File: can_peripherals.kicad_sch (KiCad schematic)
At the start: 14 parts, among them U1 MCP2515, U2 MCP2551, Y1 ABLS7M-16.000MHZ-B-2-T

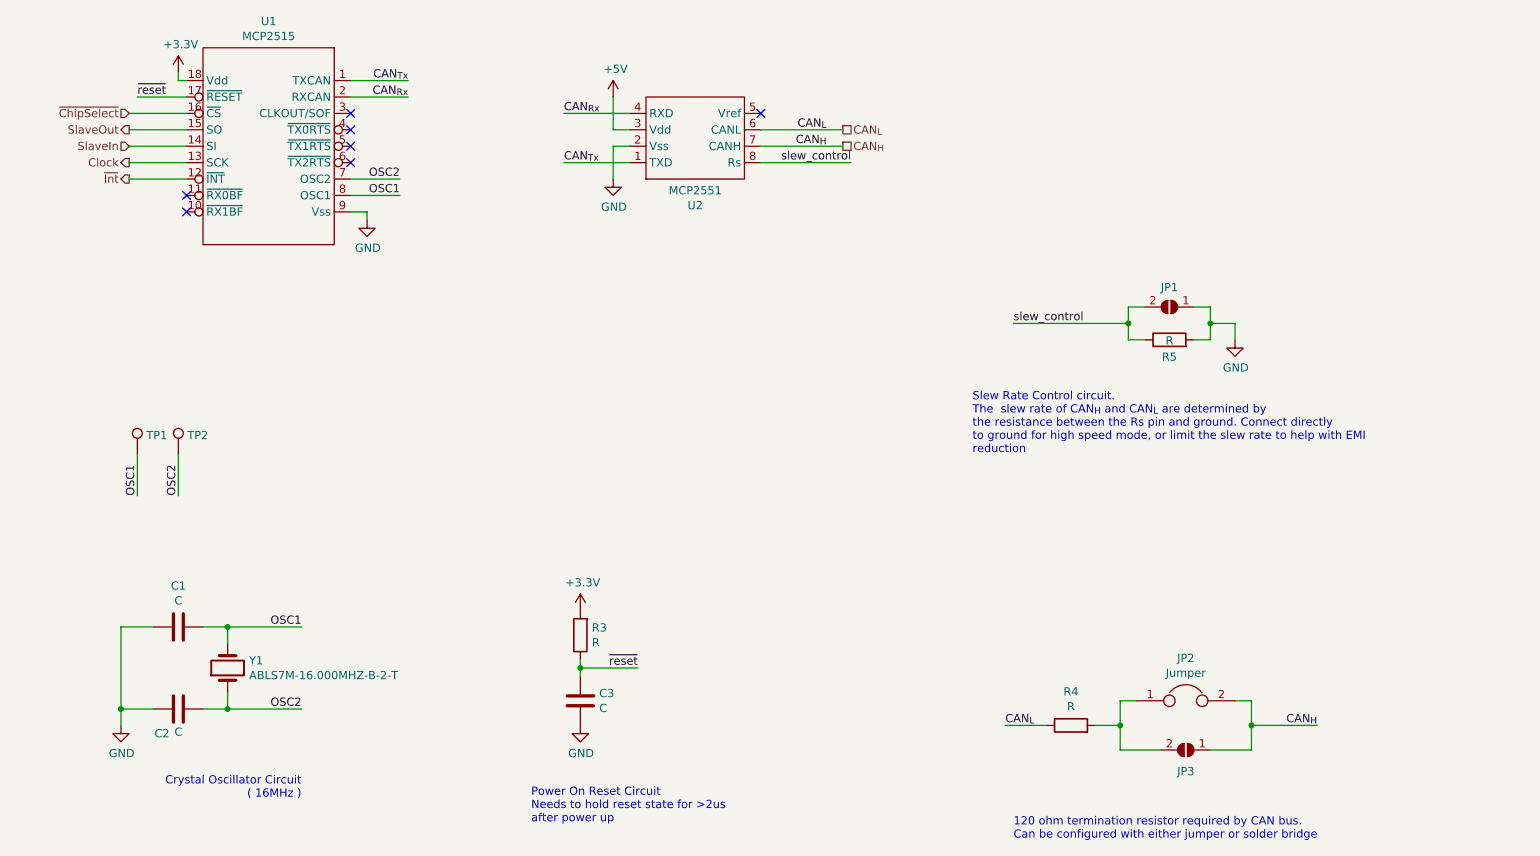
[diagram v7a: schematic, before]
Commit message: more layout: power supply and gpio
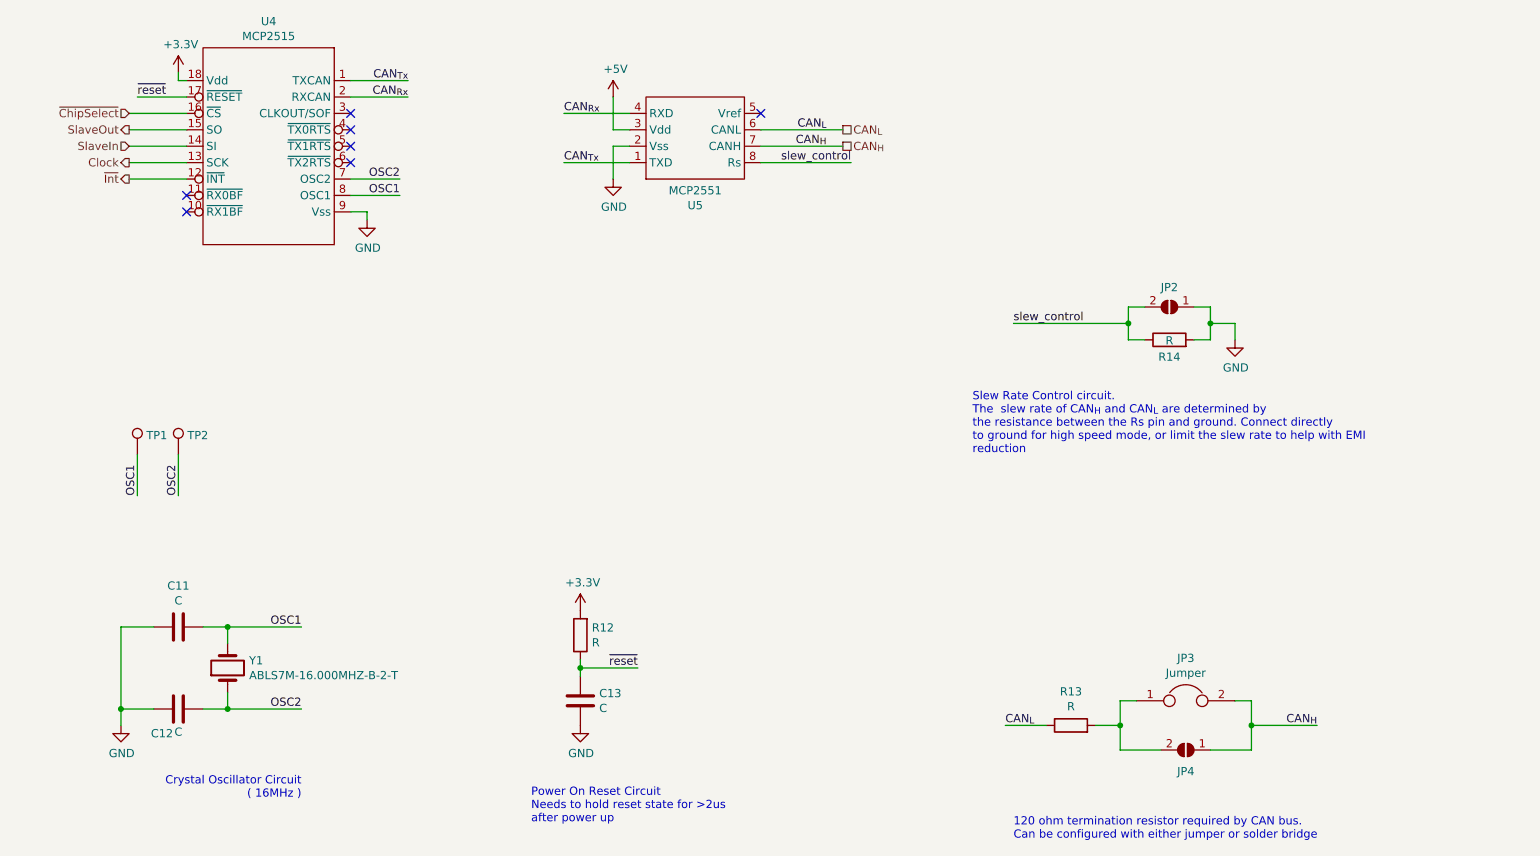
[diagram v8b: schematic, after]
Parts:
- renumbered C1 to C11, C2 to C12, C3 to C13, JP1 to JP2, JP2 to JP3, JP3 to JP4, R3 to R12, R4 to R13, R5 to R14, U1 to U4, U2 to U5
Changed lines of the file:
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@@
   (junction (at 208.026 71.882) (diameter 0.9144) (color 0 0 0 0))
   (junction (at 214.376 134.112) (diameter 0.9144) (color 0 0 0 0))
+  (no_connect (at 49.53 54.61))
+  (no_connect (at 74.93 44.45))
+  (no_connect (at 74.93 41.91))
+  (no_connect (at 74.93 39.37))
+  (no_connect (at 74.93 46.99))
+  (no_connect (at 49.53 52.07))
   (no_connect (at 138.43 39.37))
-  (no_connect (at 74.93 41.91))
-  (no_connect (at 74.93 46.99))
-  (no_connect (at 74.93 39.37))
-  (no_connect (at 49.53 52.07))
-  (no_connect (at 74.93 44.45))
-  (no_connect (at 49.53 54.61))
   (wire (pts (xy 39.37 118.872) (xy 39.37 131.572))
     (stroke (width 0) (type solid) (color 0 0 0 0))
@@
   (symbol (lib_id "power:+3.3V") (at 48.26 33.02 0) (unit 1)
     (in_bom yes) (on_board yes)
-    (property "Reference" "#PWR0113" (id 0) (at 48.26 36.83 0)
+    (property "Reference" "#PWR0148" (id 0) (at 48.26 36.83 0)
       (effects (font (size 1.27 1.27)) hide)
     )
@@
   (symbol (lib_id "power:+3.3V") (at 110.49 116.332 0) (unit 1)
     (in_bom yes) (on_board yes)
-    (property "Reference" "#PWR0118" (id 0) (at 110.49 120.142 0)
+    (property "Reference" "#PWR0144" (id 0) (at 110.49 120.142 0)
       (effects (font (size 1.27 1.27)) hide)
     )
@@
   (symbol (lib_id "power:+5V") (at 115.57 36.83 0) (unit 1)
     (in_bom yes) (on_board yes)
-    (property "Reference" "#PWR0116" (id 0) (at 115.57 40.64 0)
+    (property "Reference" "#PWR0147" (id 0) (at 115.57 40.64 0)
       (effects (font (size 1.27 1.27)) hide)
     )
@@
   (symbol (lib_id "power:GND") (at 39.37 134.112 0) (unit 1)
     (in_bom yes) (on_board yes)
-    (property "Reference" "#PWR0114" (id 0) (at 39.37 140.462 0)
+    (property "Reference" "#PWR0142" (id 0) (at 39.37 140.462 0)
       (effects (font (size 1.27 1.27)) hide)
     )
@@
   (symbol (lib_id "power:GND") (at 77.47 55.88 0) (unit 1)
     (in_bom yes) (on_board yes)
-    (property "Reference" "#PWR0119" (id 0) (at 77.47 62.23 0)
+    (property "Reference" "#PWR0145" (id 0) (at 77.47 62.23 0)
       (effects (font (size 1.27 1.27)) hide)
     )
@@
   (symbol (lib_id "power:GND") (at 110.49 134.112 0) (unit 1)
     (in_bom yes) (on_board yes)
-    (property "Reference" "#PWR0117" (id 0) (at 110.49 140.462 0)
+    (property "Reference" "#PWR0143" (id 0) (at 110.49 140.462 0)
       (effects (font (size 1.27 1.27)) hide)
     )
@@
   (symbol (lib_id "power:GND") (at 115.57 49.53 0) (unit 1)
     (in_bom yes) (on_board yes)
-    (property "Reference" "#PWR0115" (id 0) (at 115.57 55.88 0)
+    (property "Reference" "#PWR0146" (id 0) (at 115.57 55.88 0)
       (effects (font (size 1.27 1.27)) hide)
     )
@@
   (symbol (lib_id "power:GND") (at 211.836 74.422 0) (unit 1)
     (in_bom yes) (on_board yes)
-    (property "Reference" "#PWR0112" (id 0) (at 211.836 80.772 0)
+    (property "Reference" "#PWR0141" (id 0) (at 211.836 80.772 0)
       (effects (font (size 1.27 1.27)) hide)
     )
@@
   (symbol (lib_id "Device:R") (at 110.49 120.142 180) (unit 1)
     (in_bom yes) (on_board yes)
-    (property "Reference" "R3" (id 0) (at 112.2681 118.9926 0)
+    (property "Reference" "R12" (id 0) (at 112.2681 118.9926 0)
       (effects (font (size 1.27 1.27)) (justify right))
     )
@@
   (symbol (lib_id "Device:R") (at 186.436 134.112 90) (unit 1)
     (in_bom yes) (on_board yes)
-    (property "Reference" "R4" (id 0) (at 186.436 128.8858 90))
+    (property "Reference" "R13" (id 0) (at 186.436 128.8858 90))
     (property "Value" "R" (id 1) (at 186.436 131.1845 90))
     (property "Footprint" "Resistor_SMD:R_0805_2012Metric" (id 2) (at 186.436 135.89 90)
@@
   (symbol (lib_id "Device:R") (at 201.676 74.422 90) (unit 1)
     (in_bom yes) (on_board yes)
-    (property "Reference" "R5" (id 0) (at 201.676 77.0698 90))
+    (property "Reference" "R14" (id 0) (at 201.676 77.0698 90))
     (property "Value" "R" (id 1) (at 201.676 74.5425 90))
     (property "Footprint" "Resistor_SMD:R_0805_2012Metric" (id 2) (at 201.676 76.2 90)
@@
   (symbol (lib_id "Jumper:SolderJumper_2_Open") (at 201.676 69.342 180) (unit 1)
     (in_bom yes) (on_board yes)
-    (property "Reference" "JP1" (id 0) (at 201.676 66.3002 0))
+    (property "Reference" "JP2" (id 0) (at 201.676 66.3002 0))
     (property "Value" "SolderJumper_2_Open" (id 1) (at 201.676 76.219 0)
       (effects (font (size 1.27 1.27)) hide)
@@
   (symbol (lib_id "Jumper:SolderJumper_2_Open") (at 204.216 137.922 180) (unit 1)
     (in_bom yes) (on_board yes)
-    (property "Reference" "JP3" (id 0) (at 204.216 141.2302 0))
+    (property "Reference" "JP4" (id 0) (at 204.216 141.2302 0))
     (property "Value" "SolderJumper_2_Open" (id 1) (at 204.216 144.799 0)
       (effects (font (size 1.27 1.27)) hide)
@@
   (symbol (lib_id "Device:C") (at 48.26 118.872 270) (mirror x) (unit 1)
     (in_bom yes) (on_board yes)
-    (property "Reference" "C1" (id 0) (at 48.26 112.5028 90))
+    (property "Reference" "C11" (id 0) (at 48.26 112.5028 90))
     (property "Value" "C" (id 1) (at 48.26 114.8015 90))
     (property "Footprint" "Capacitor_SMD:C_0805_2012Metric" (id 2) (at 44.45 117.9068 0)
@@
   (symbol (lib_id "Device:C") (at 48.26 131.572 270) (mirror x) (unit 1)
     (in_bom yes) (on_board yes)
-    (property "Reference" "C2" (id 0) (at 45.72 135.3628 90))
+    (property "Reference" "C12" (id 0) (at 45.72 135.3628 90))
     (property "Value" "C" (id 1) (at 48.26 135.1215 90))
     (property "Footprint" "Capacitor_SMD:C_0805_2012Metric" (id 2) (at 44.45 130.6068 0)
@@
   (symbol (lib_id "Device:C") (at 110.49 130.302 0) (unit 1)
     (in_bom yes) (on_board yes)
-    (property "Reference" "C3" (id 0) (at 113.4111 129.1526 0)
+    (property "Reference" "C13" (id 0) (at 113.4111 129.1526 0)
       (effects (font (size 1.27 1.27)) (justify left))
     )
@@
   (symbol (lib_id "Device:Jumper") (at 204.216 130.302 0) (unit 1)
     (in_bom yes) (on_board yes)
-    (property "Reference" "JP2" (id 0) (at 204.216 123.7042 0))
+    (property "Reference" "JP3" (id 0) (at 204.216 123.7042 0))
     (property "Value" "Jumper" (id 1) (at 204.216 126.0029 0))
     (property "Footprint" "Connector_PinHeader_2.54mm:PinHeader_1x02_P2.54mm_Vertical" (id 2) (at 204.216 130.302 0)
@@
   (symbol (lib_id "symbols:MCP2551") (at 128.27 41.91 0) (mirror x) (unit 1)
     (in_bom yes) (on_board yes)
-    (property "Reference" "U2" (id 0) (at 128.27 53.6132 0))
+    (property "Reference" "U5" (id 0) (at 128.27 53.6132 0))
     (property "Value" "MCP2551" (id 1) (at 128.27 51.3145 0))
     (property "Footprint" "Package_SO:SO-8_3.9x4.9mm_P1.27mm" (id 2) (at 133.35 72.39 0)
@@
   (symbol (lib_id "symbols:MCP2515") (at 62.23 44.45 0) (mirror y) (unit 1)
     (in_bom yes) (on_board yes)
-    (property "Reference" "U1" (id 0) (at 62.23 25.1268 0))
+    (property "Reference" "U4" (id 0) (at 62.23 25.1268 0))
     (property "Value" "MCP2515" (id 1) (at 62.23 27.4255 0))
     (property "Footprint" "Package_SO:SOIC-18W_7.5x11.6mm_P1.27mm" (id 2) (at 57.15 13.97 0)
